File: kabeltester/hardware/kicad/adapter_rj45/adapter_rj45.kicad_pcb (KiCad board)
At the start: 2 copper layers, 100 x 60 mm, 7 parts, among them J1 DIN 41612 C96 Messer, J2 RJ45 Port 1, J3 RJ45 Port 2, U1 24AA02T-I/OT

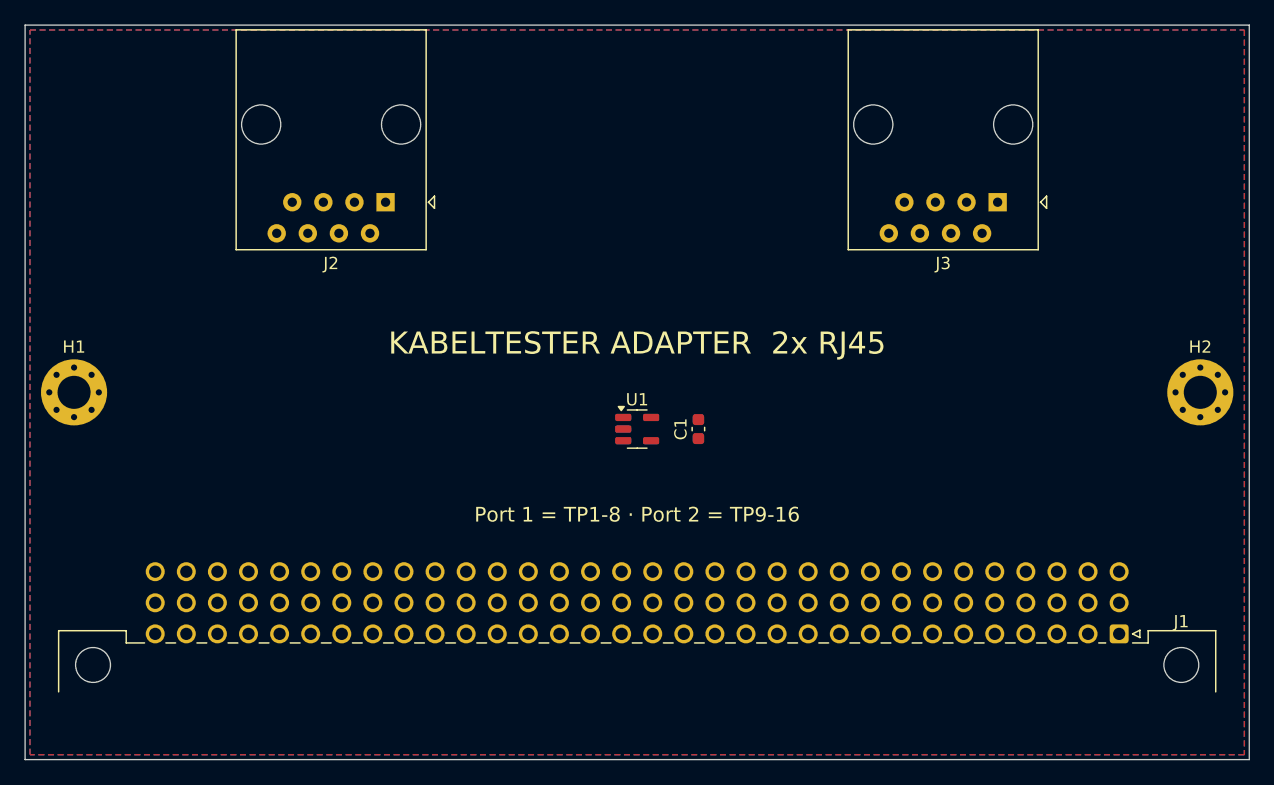
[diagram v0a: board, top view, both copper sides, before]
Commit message: Adapter-Platine vollständig geroutet (DRC 0 Fehler), SES-Import und Masse-Vias im Generator
- routen.py: Freerouting auf vorhandener Platine, eigener SES-Import (KiCad 7 kann das in Python nicht)
- Masseflächen mit voller Anbindung, Masse-Durchkontaktierungen im Raster
- Adapter: Reservepins b9/b10 unbeschaltet (zweilagig nicht anbindbar)

Co-Authored-By: Claude Opus 5.5 <noreply@anthropic.com>
Claude-Session: https://claude.ai/code/session_0119zGeGQCWTR3UwpEi96iWe
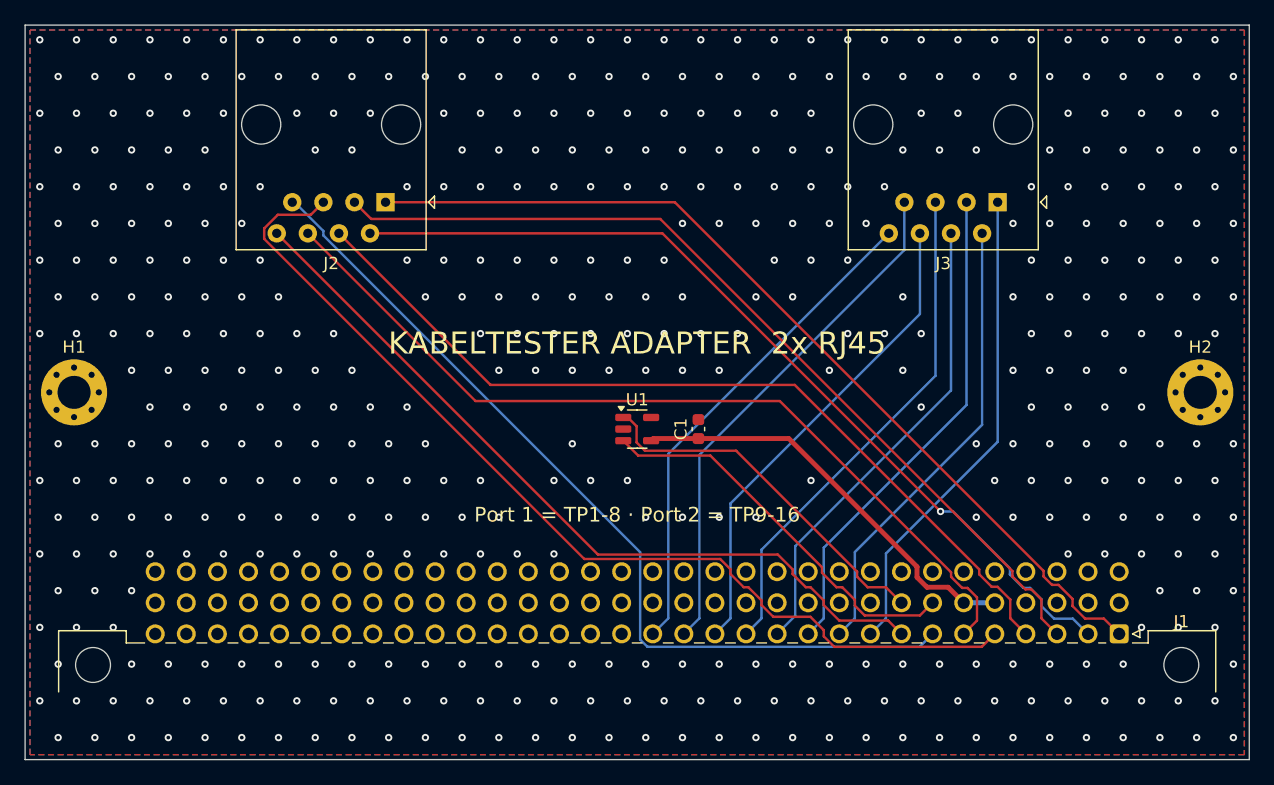
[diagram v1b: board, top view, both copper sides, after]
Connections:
- J1 pad b10: GND -> (no net)
- J1 pad b9: GND -> (no net)
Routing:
- net TP5: track 0.00 -> 81.2 mm
- net TP1: track 0.00 -> 75.1 mm
- net TP3: track 0.00 -> 73.2 mm
- net TP2: track 0.00 -> 72.8 mm, vias 0 -> 1
- net TP7: track 0.00 -> 72.2 mm
- net TP4: track 0.00 -> 70.8 mm
- net TP6: track 0.00 -> 70.6 mm
- net TP8: track 0.00 -> 65.0 mm
- net TP15: track 0.00 -> 42.7 mm
- net TP13: track 0.00 -> 41.7 mm
- net TP16: track 0.00 -> 40.7 mm
- net TP11: track 0.00 -> 40.6 mm
- net TP14: track 0.00 -> 39.7 mm
- net TP9: track 0.00 -> 39.6 mm
- net TP12: track 0.00 -> 38.6 mm
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
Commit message: Routing: Adapter vollständig (DRC 0), Messkarte bis auf 17 Verbindungen
- Adapter 2x RJ45: 0 DRC-Fehler, 0 offene Verbindungen, 174 Masse-Vias
- Messkarte: 297 -> 17 offen (13 kleine GND-Inseln ohne Via-Platz, 4 Signalnetze)
- Generator: Masse-Fanout für unverbundene GND-Pads, Via je Masseinsel, GND-Fläche oben

Co-Authored-By: Claude Opus 5.5 <noreply@anthropic.com>
Claude-Session: https://claude.ai/code/session_0119zGeGQCWTR3UwpEi96iWe
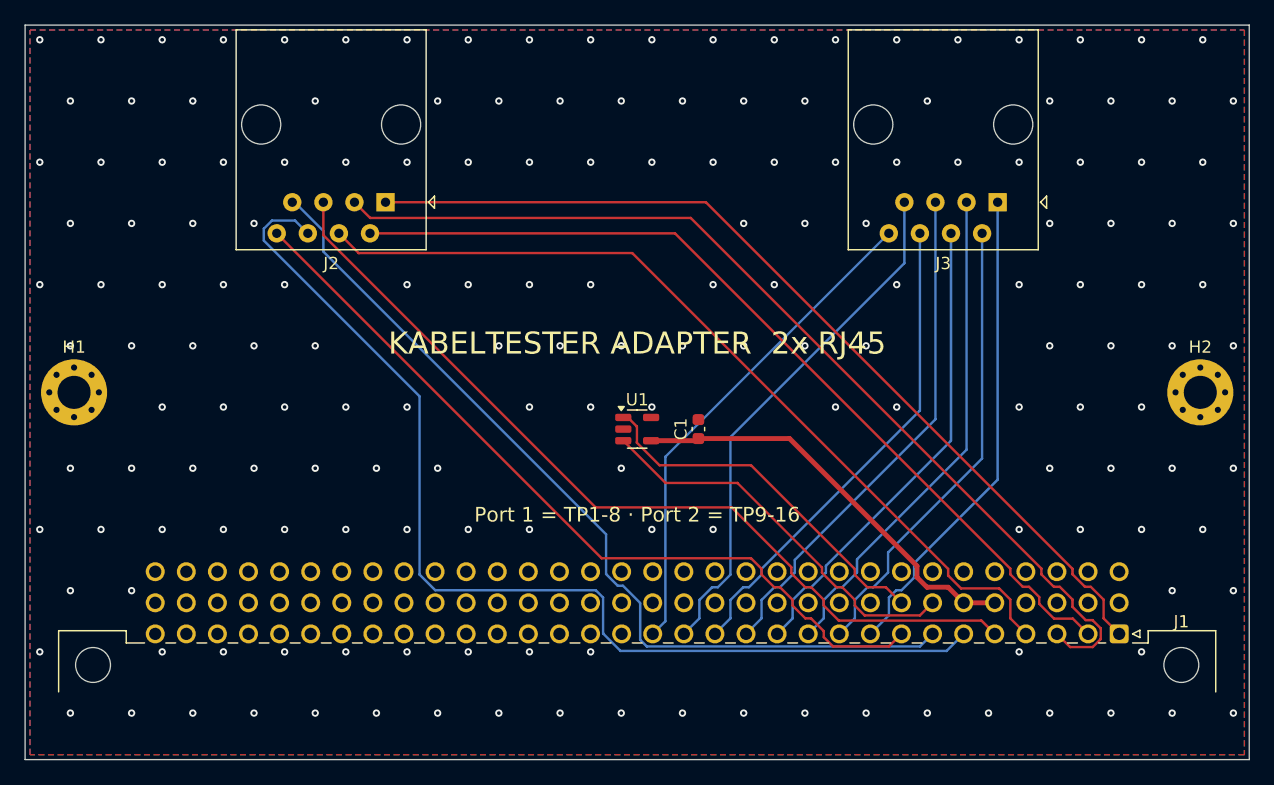
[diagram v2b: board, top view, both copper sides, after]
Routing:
- net TP6: track 70.6 -> 87.2 mm
- net TP5: track 81.2 -> 71.6 mm
- net TP3: track 73.2 -> 81.2 mm
- net TP8: track 65.0 -> 66.3 mm
- net TP1: track 75.1 -> 75.7 mm
- net TP2: vias 1 -> 0
- net GND: vias 471 -> 174
